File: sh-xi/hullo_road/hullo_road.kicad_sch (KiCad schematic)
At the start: 139 parts

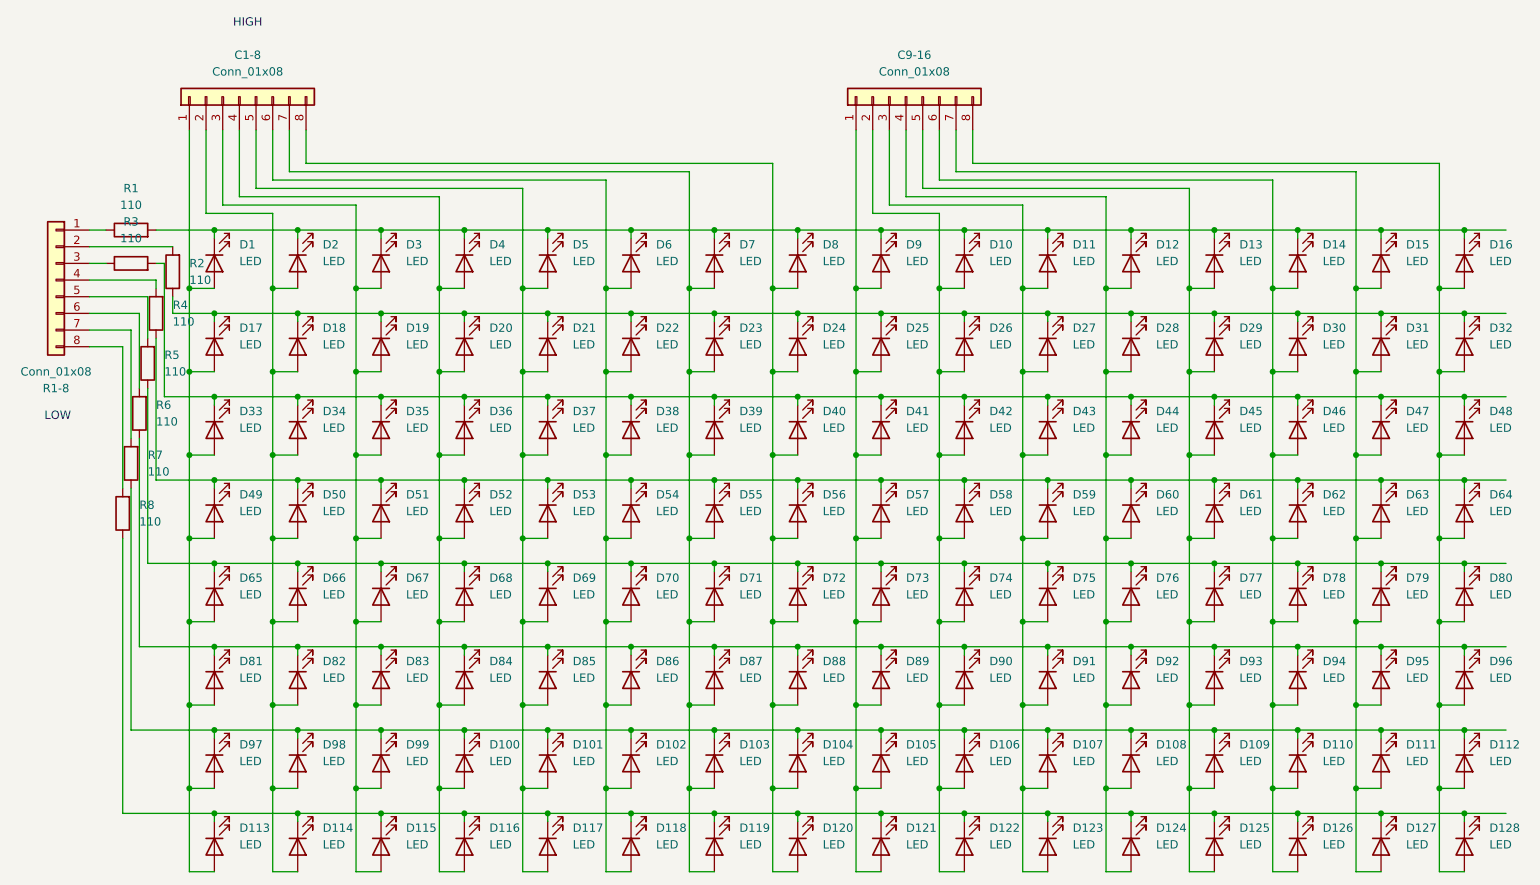
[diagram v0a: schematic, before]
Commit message: Add LED matrix
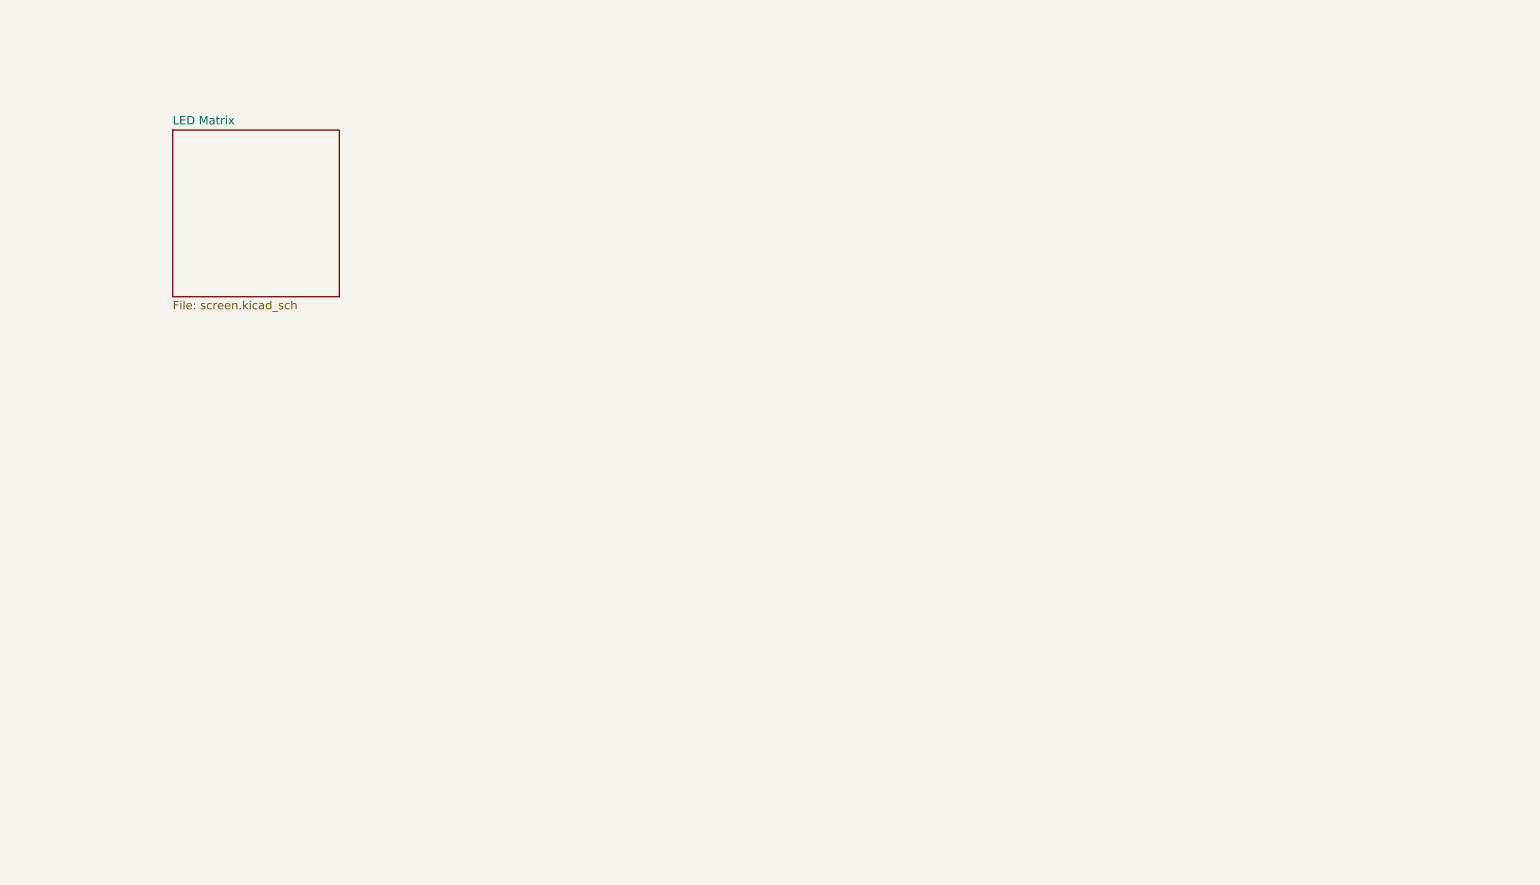
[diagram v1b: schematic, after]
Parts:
- removed C1-8, C9-16, R1-8: Conn_01x08, Connector_PinHeader_2.54mm:PinHeader_1x08_P2.54mm_Vertical, symbol Connector_Generic:Conn_01x08
- removed D1, D10, D100, D101, D102, D103, D104, D105, D106, D107, D108, D109, D11, D110, D111, D112, D113, D114, D115, D116, D117, D118, D119, D12, D120, D121, D122, D123, D124, D125, D126, D127, D128, D13, D14, D15, D16, D17, D18, D19, D2, D20, D21, D22, D23, D24, D25, D26, D27, D28, D29, D3, D30, D31, D32, D33, D34, D35, D36, D37, D38, D39, D4, D40, D41, D42, D43, D44, D45, D46, D47, D48, D49, D5, D50, D51, D52, D53, D54, D55, D56, D57, D58, D59, D6, D60, D61, D62, D63, D64, D65, D66, D67, D68, D69, D7, D70, D71, D72, D73, D74, D75, D76, D77, D78, D79, D8, D80, D81, D82, D83, D84, D85, D86, D87, D88, D89, D9, D90, D91, D92, D93, D94, D95, D96, D97, D98, D99: LED, LED_SMD:LED_0603_1608Metric, symbol Device:LED
- removed R1, R2, R3, R4, R5, R6, R7, R8: 110, Resistor_THT:R_Axial_DIN0207_L6.3mm_D2.5mm_P10.16mm_Horizontal, symbol Device:R
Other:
- added sheet LED Matrix (screen.kicad_sch)
- note removed: "HIGH"
- note removed: "LOW"

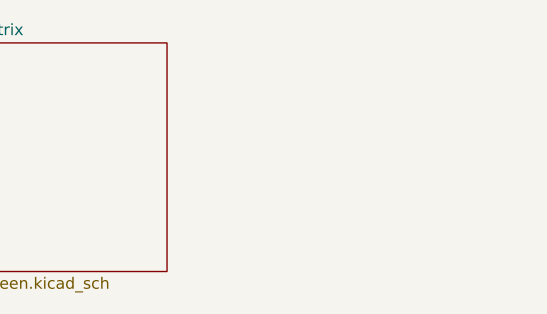
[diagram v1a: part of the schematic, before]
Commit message: Add matrix control via shift registers and attiny414
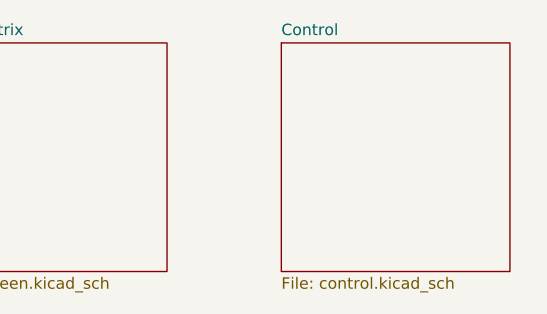
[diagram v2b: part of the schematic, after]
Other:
- added sheet Control (control.kicad_sch)
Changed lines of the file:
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@@
+		)
+	)
+	(sheet
+		(at 76.2 38.1)
+		(size 25.4 25.4)
+		(exclude_from_sim no)
+		(in_bom yes)
+		(on_board yes)
+		(dnp no)
+		(fields_autoplaced yes)
+		(stroke
+			(width 0.1524)
+			(type solid)
+		)
+		(fill
+			(color 0 0 0 0.0000)
+		)
+		(property "Sheetname" "Control"
+			(at 76.2 37.3884 0)
+			(effects
+				(font
+					(size 1.27 1.27)
+				)
+				(justify left bottom)
+			)
+		)
+		(property "Sheetfile" "control.kicad_sch"
+			(at 76.2 64.0846 0)
+			(effects
+				(font
+					(size 1.27 1.27)
+				)
+				(justify left top)
+			)
+		)
+		(instances
+			(project "hullo_road"
+				(path "/be742489-42fa-4524-ab86-4a70063d0740"
+					(page "3")
+				)
+			)
 		)
 	)
